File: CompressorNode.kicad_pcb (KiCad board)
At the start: 2 copper layers, 129.5 x 85.1 mm, 33 parts, among them J1 EXT1, J10 Screw_Terminal_01x03, J11 Screw_Terminal_01x02, J12 Screw_Terminal_01x03, J13 Screw_Terminal_01x04, J2 Screw_Terminal_01x04, J3 Screw_Terminal_01x03, J4 EXT2, J5 Screw_Terminal_01x02, J6 Screw_Terminal_01x02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

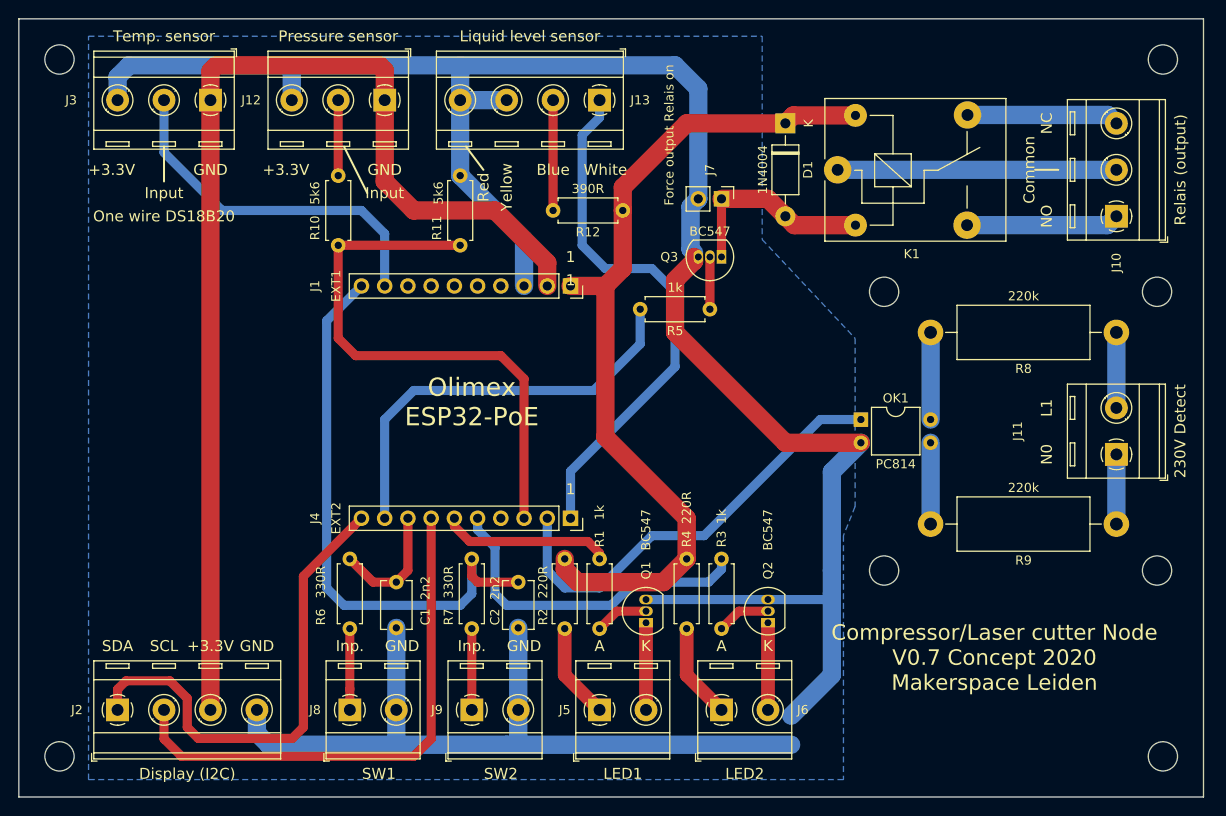
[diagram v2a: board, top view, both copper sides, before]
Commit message: LED Resistnow 47R to increase current for high power LEDs
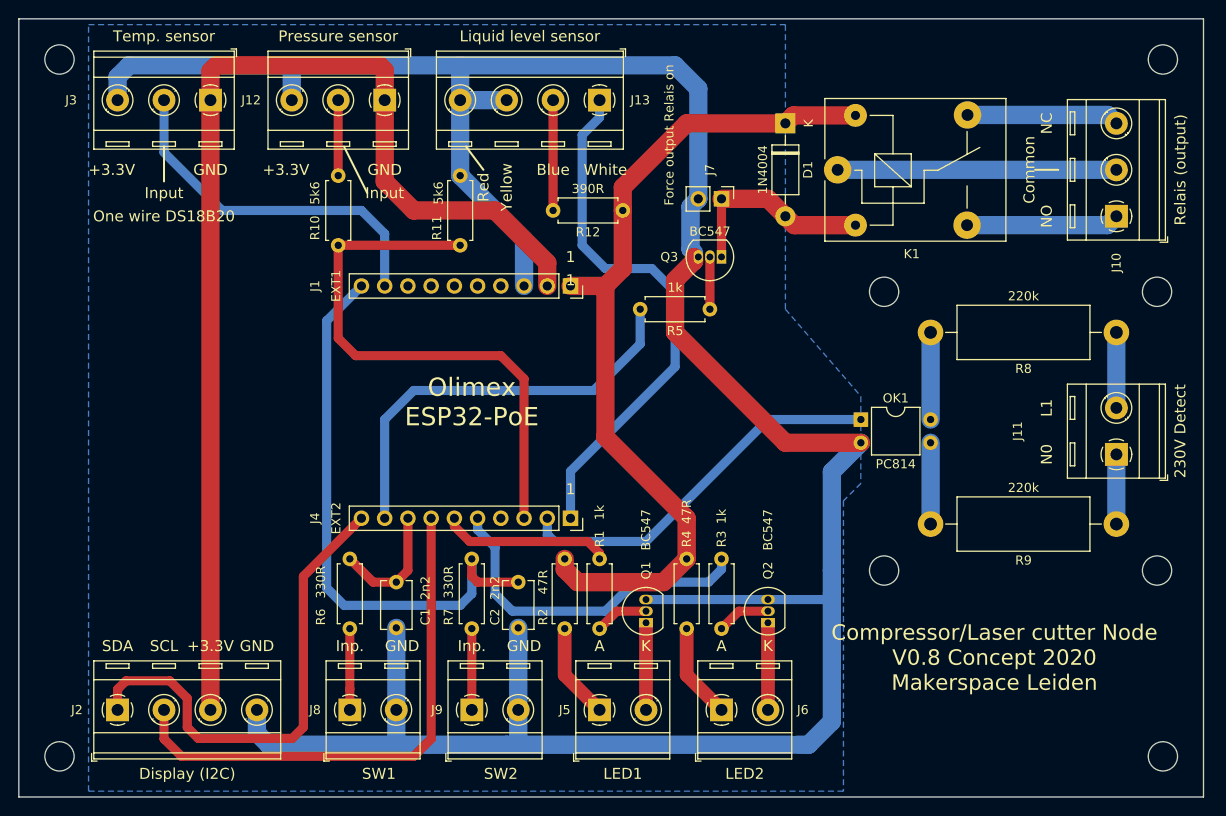
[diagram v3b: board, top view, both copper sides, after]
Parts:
- R2, R4: value 220R -> 47R
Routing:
- net GPI36_U1RXD: track 48.4 -> 42.0 mm
- net GND: track 297.1 -> 300.7 mm
- net GPIO33: track 37.1 -> 37.6 mm
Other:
- board text added: "Compressor/Laser cutter Node V0.8 Concept 2020 Makerspace Leiden"
- board text removed: "Compressor/Laser cutter Node V0.7 Concept 2020 Makerspace Leiden"
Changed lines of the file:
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@@
   (title_block
     (title CompressorNode)
-    (date 2020-03-29)
-    (rev "V0.7 Concept")
+    (date 2020-03-30)
+    (rev "V0.8 Concept")
     (company "MakerSpace Leiden")
     (comment 1 "Getekend door Hans Beerman")
@@
   )
   (setup
-    (last_trace_width 2)
+    (last_trace_width 0.25)
     (user_trace_width 0.5)
     (user_trace_width 0.75)
@@
     (add_net +3V3)
     (add_net +5V)
+    (add_net ESP_EN)
     (add_net GND)
+    (add_net GPI34_BUT1)
     (add_net GPI35)
     (add_net GPI36_U1RXD)
     (add_net GPI39)
+    (add_net GPIO0)
     (add_net GPIO13_I2C-SDA)
     (add_net GPIO14_HS2_CLK)
     (add_net GPIO15_HS2_CMD)
     (add_net GPIO16_I2C-SCL)
+    (add_net GPIO1_U0TXD)
+    (add_net GPIO2_HS2_DATA0)
     (add_net GPIO32)
     (add_net GPIO33)
+    (add_net GPIO3_U0RXD)
     (add_net GPIO4_U1TXD)
     (add_net GPIO5_SPI_C5)
@@
       (effects (font (size 1 1) (thickness 0.15)) (justify left))
     )
-    (fp_text value 220R (at -3.81 0 90) (layer F.SilkS)
+    (fp_text value 47R (at -3.81 0 90) (layer F.SilkS)
       (effects (font (size 1 1) (thickness 0.15)) (justify left))
     )
@@
       (effects (font (size 1 1) (thickness 0.15)))
     )
-    (fp_text value 220R (at 2.54 2.37 90) (layer F.SilkS)
+    (fp_text value 47R (at 2.54 2.37 90) (layer F.SilkS)
       (effects (font (size 1 1) (thickness 0.15)))
     )
@@
     (effects (font (size 1.2 1.2) (thickness 0.3)))
   )
-  (gr_text "Compressor/Laser cutter Node\nV0.7 Concept 2020\nMakerspace Leiden" (at 190.5 124.46) (layer F.SilkS)
+  (gr_text "Compressor/Laser cutter Node\nV0.8 Concept 2020\nMakerspace Leiden" (at 190.5 124.46) (layer F.SilkS)
     (effects (font (size 1.7 1.7) (thickness 0.4)))
   )
@@
   (segment (start 167.64 100.965) (end 155.575 88.9) (width 2) (layer F.Cu) (net 1))
   (segment (start 138.43 130.175) (end 138.43 121.205) (width 2) (layer B.Cu) (net 1))
-  (segment (start 168.275 130.81) (end 172.72 126.365) (width 2) (layer B.Cu) (net 1))
   (segment (start 172.72 104.14) (end 175.895 100.965) (width 2) (layer B.Cu) (net 1))
   (segment (start 138.43 130.175) (end 138.43 133.985) (width 2) (layer B.Cu) (net 1))
@@
   (segment (start 172.085 118.11) (end 172.72 117.475) (width 1) (layer B.Cu) (net 1))
   (segment (start 152.4 118.11) (end 172.085 118.11) (width 1) (layer B.Cu) (net 1))
-  (segment (start 172.72 126.365) (end 172.72 117.475) (width 2) (layer B.Cu) (net 1))
   (segment (start 172.72 117.475) (end 172.72 114.935) (width 2) (layer B.Cu) (net 1))
+  (segment (start 172.72 131.445) (end 172.72 117.475) (width 2) (layer B.Cu) (net 1))
+  (segment (start 168.91 133.985) (end 170.18 133.985) (width 2) (layer B.Cu) (net 1))
+  (segment (start 170.18 133.985) (end 172.72 131.445) (width 2) (layer B.Cu) (net 1))
   (segment (start 126.365 114.935) (end 125.095 116.205) (width 1) (layer F.Cu) (net 2))
   (segment (start 122.555 116.205) (end 120.015 113.665) (width 1) (layer F.Cu) (net 2))
@@
   (segment (start 147.32 113.03) (end 146.05 111.76) (width 1) (layer F.Cu) (net 11))
   (segment (start 133.985 110.49) (end 133.985 109.22) (width 1) (layer B.Cu) (net 12))
+  (segment (start 135.89 112.395) (end 133.985 110.49) (width 1) (layer B.Cu) (net 12))
   (segment (start 135.89 117.475) (end 135.89 112.395) (width 1) (layer B.Cu) (net 12))
   (segment (start 160.655 114.79637) (end 159.24637 116.205) (width 1) (layer B.Cu) (net 12))
+  (segment (start 147.955 119.38) (end 137.795 119.38) (width 1) (layer B.Cu) (net 12))
+  (segment (start 137.795 119.38) (end 135.89 117.475) (width 1) (layer B.Cu) (net 12))
+  (segment (start 159.24637 116.205) (end 151.13 116.205) (width 1) (layer B.Cu) (net 12))
   (segment (start 160.655 113.665) (end 160.655 114.79637) (width 1) (layer B.Cu) (net 12))
-  (segment (start 135.89 112.395) (end 133.985 110.49) (width 1) (layer B.Cu) (net 12))
-  (segment (start 159.24637 116.205) (end 151.13 116.205) (width 1) (layer B.Cu) (net 12))
-  (segment (start 151.13 116.205) (end 148.59 118.745) (width 1) (layer B.Cu) (net 12))
-  (segment (start 148.59 118.745) (end 137.16 118.745) (width 1) (layer B.Cu) (net 12))
-  (segment (start 137.16 118.745) (end 135.89 117.475) (width 1) (layer B.Cu) (net 12))
+  (segment (start 151.13 116.205) (end 147.955 119.38) (width 1) (layer B.Cu) (net 12))
   (segment (start 118.745 79.375) (end 132.08 79.375) (width 1) (layer F.Cu) (net 13))
   (segment (start 136.525 91.44) (end 139.065 93.98) (width 1) (layer F.Cu) (net 13))
@@
   (segment (start 118.745 89.535) (end 120.65 91.44) (width 1) (layer F.Cu) (net 13))
   (segment (start 141.605 110.422081) (end 141.605 109.22) (width 1) (layer B.Cu) (net 14))
-  (segment (start 141.605 114.935) (end 141.605 110.422081) (width 1) (layer B.Cu) (net 14))
-  (segment (start 171.45 98.425) (end 158.75 111.125) (width 1) (layer B.Cu) (net 14))
-  (segment (start 175.895 98.425) (end 171.45 98.425) (width 1) (layer B.Cu) (net 14))
-  (segment (start 158.75 111.125) (end 153.035 111.125) (width 1) (layer B.Cu) (net 14))
-  (segment (start 153.035 111.125) (end 147.32 116.84) (width 1) (layer B.Cu) (net 14))
-  (segment (start 143.51 116.84) (end 141.605 114.935) (width 1) (layer B.Cu) (net 14))
-  (segment (start 147.32 116.84) (end 143.51 116.84) (width 1) (layer B.Cu) (net 14))
+  (segment (start 175.895 98.425) (end 165.735 98.425) (width 1) (layer B.Cu) (net 14))
+  (segment (start 152.4 111.76) (end 142.385 111.76) (width 1) (layer B.Cu) (net 14))
+  (segment (start 142.385 111.76) (end 141.75 111.125) (width 1) (layer B.Cu) (net 14))
+  (segment (start 141.605 111.125) (end 141.605 110.422081) (width 1) (layer B.Cu) (net 14))
+  (segment (start 165.735 98.425) (end 152.4 111.76) (width 1) (layer B.Cu) (net 14))
+  (segment (start 141.75 111.125) (end 141.605 111.125) (width 1) (layer B.Cu) (net 14))
   (segment (start 147.32 65.405) (end 145.415 67.31) (width 1) (layer B.Cu) (net 15))
   (segment (start 145.415 79.375) (end 147.955 81.915) (width 1) (layer B.Cu) (net 15))
@@
     (polygon
       (pts
-        (xy 165.1 78.74) (xy 175.26 89.535) (xy 175.26 107.95) (xy 173.99 111.125) (xy 173.99 137.795)
-        (xy 91.44 137.795) (xy 91.44 56.515) (xy 165.1 56.515)
+        (xy 167.64 86.36) (xy 175.895 95.885) (xy 175.895 105.41) (xy 173.99 107.315) (xy 173.99 139.065)
+        (xy 91.44 139.065) (xy 91.44 55.245) (xy 167.64 55.245)
       )
     )

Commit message: Optocoupler was connected wrong
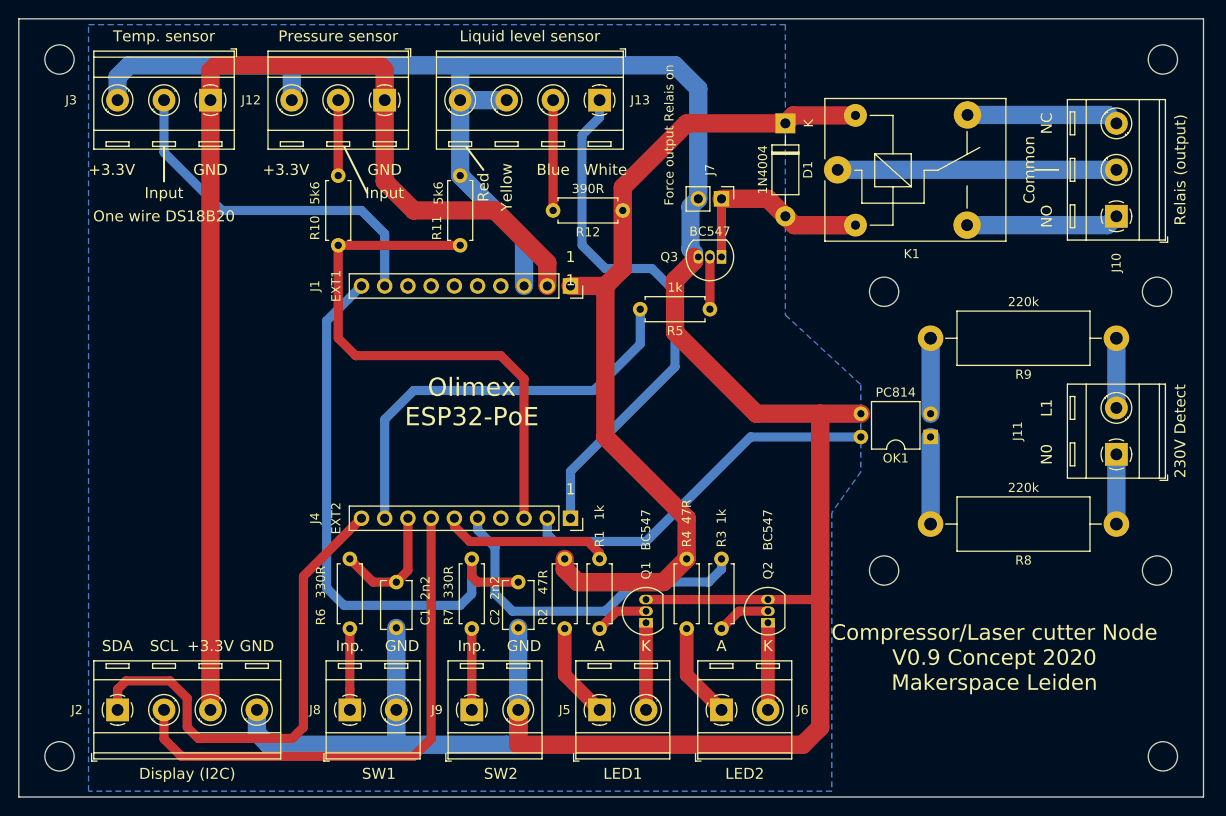
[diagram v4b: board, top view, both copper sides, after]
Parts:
- moved R8 21.0 mm to (203.8, 109.9)
- moved R9 20.3 mm to (203.8, 89.5)
- moved OK1 7.85 mm to (183.5, 100.3), turned to 180 degrees
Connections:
- OK1 pad 1: GPI36_U1RXD -> Net-(OK1-Pad1)
- OK1 pad 2: GND -> Net-(OK1-Pad2)
- OK1 pad 3: Net-(OK1-Pad3) -> GND
- OK1 pad 4: Net-(OK1-Pad4) -> GPI36_U1RXD
- R8 pad 1: Net-(J11-Pad2) -> Net-(J11-Pad1)
- R8 pad 2: Net-(OK1-Pad4) -> Net-(OK1-Pad1)
- R9 pad 1: Net-(J11-Pad1) -> Net-(J11-Pad2)
- R9 pad 2: Net-(OK1-Pad3) -> Net-(OK1-Pad2)
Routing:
- net Net-(OK1-Pad1): track 0.00 -> 9.53 mm
- net Net-(OK1-Pad4): track 9.52 -> 0.00 mm
- net Net-(OK1-Pad3): track 8.89 -> 0.00 mm
- net Net-(OK1-Pad2): track 0.00 -> 8.26 mm
- net GND: track 300.7 -> 303.3 mm
- net GPI36_U1RXD: track 42.0 -> 41.2 mm
- net Net-(J11-Pad2): track 8.25 -> 7.62 mm
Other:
- board text added: "Compressor/Laser cutter Node V0.9 Concept 2020 Makerspace Leiden"
- board text removed: "Compressor/Laser cutter Node V0.8 Concept 2020 Makerspace Leiden"

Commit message: R5 is now 150R because relais uses more current than expected
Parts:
- R5: value 1k -> 150R
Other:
- board text added: "Compressor/Laser cutter Node V0.10 Concept 2020 Makerspace Leiden"
- board text removed: "Compressor/Laser cutter Node V0.9 Concept 2020 Makerspace Leiden"
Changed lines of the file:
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@@
     (title CompressorNode)
     (date 2020-04-01)
-    (rev "V0.9 Concept")
+    (rev "V0.10 Concept")
     (company "MakerSpace Leiden")
     (comment 1 "Getekend door Hans Beerman")
@@
   )
   (setup
-    (last_trace_width 1)
+    (last_trace_width 0.25)
     (user_trace_width 0.5)
     (user_trace_width 0.75)
@@
       (effects (font (size 1 1) (thickness 0.15)))
     )
-    (fp_text value 1k (at 3.81 2.37) (layer F.SilkS)
+    (fp_text value 150R (at 3.81 2.37) (layer F.SilkS)
       (effects (font (size 1 1) (thickness 0.15)))
     )
@@
     (effects (font (size 1.2 1.2) (thickness 0.3)))
   )
-  (gr_text "Compressor/Laser cutter Node\nV0.9 Concept 2020\nMakerspace Leiden" (at 190.5 124.46) (layer F.SilkS)
+  (gr_text "Compressor/Laser cutter Node\nV0.10 Concept 2020\nMakerspace Leiden" (at 190.5 124.46) (layer F.SilkS)
     (effects (font (size 1.7 1.7) (thickness 0.4)))
   )

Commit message: resistor 4k7 added for DS18B20 temperature sensor
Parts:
- added R13: 4k7, Resistor_THT:R_Axial_DIN0207_L6.3mm_D2.5mm_P7.62mm_Horizontal, F.Cu at (128.3, 88.9)
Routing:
- net +3V3: track 125.5 -> 135.2 mm
- net GPIO4_U1TXD: track 39.2 -> 47.7 mm
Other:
- board text added: "Compressor/Laser cutter Node V0.11 Concept 2020 Makerspace Leiden"
- board text removed: "Compressor/Laser cutter Node V0.10 Concept 2020 Makerspace Leiden"
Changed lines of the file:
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@@
     (thickness 1.6)
     (drawings 59)
-    (tracks 170)
+    (tracks 176)
     (zones 0)
-    (modules 33)
+    (modules 34)
     (nets 34)
   )
@@
   (title_block
     (title CompressorNode)
-    (date 2020-04-01)
-    (rev "V0.10 Concept")
+    (date 2020-04-02)
+    (rev "V0.11 Concept")
     (company "MakerSpace Leiden")
     (comment 1 "Getekend door Hans Beerman")
@@
   )
   (setup
-    (last_trace_width 0.25)
+    (last_trace_width 1)
     (user_trace_width 0.5)
     (user_trace_width 0.75)
@@
     (add_net "Net-(Q2-Pad2)")
     (add_net "Net-(Q3-Pad2)")
+  )
+  (module Resistor_THT:R_Axial_DIN0207_L6.3mm_D2.5mm_P7.62mm_Horizontal (layer F.Cu)
+    (at 128.27 88.9)
+    (descr "Resistor, Axial_DIN0207 series, Axial, Horizontal, pin pitch=7.62mm, 0.25W = 1/4W, length*diameter=6.3*2.5mm^2, http://cdn-reichelt.de/documents/datenblatt/B400/1_4W%23YAG.pdf")
+    (tags "Resistor Axial_DIN0207 series Axial Horizontal pin pitch 7.62mm 0.25W = 1/4W length 6.3mm diameter 2.5mm")
+    (fp_text reference R13 (at 3.81 -2.37) (layer F.SilkS)
+      (effects (font (size 1 1) (thickness 0.15)))
+    )
+    (fp_text value 4k7 (at 3.81 2.37) (layer F.SilkS)
+      (effects (font (size 1 1) (thickness 0.15)))
+    )
+    (fp_text user %R (at 3.81 0) (layer F.Fab)
+      (effects (font (size 1 1) (thickness 0.15)))
+    )
+    (fp_line (start 8.67 -1.5) (end -1.05 -1.5) (layer F.CrtYd) (width 0.05))
+    (fp_line (start 8.67 1.5) (end 8.67 -1.5) (layer F.CrtYd) (width 0.05))
+    (fp_line (start -1.05 1.5) (end 8.67 1.5) (layer F.CrtYd) (width 0.05))
+    (fp_line (start -1.05 -1.5) (end -1.05 1.5) (layer F.CrtYd) (width 0.05))
+    (fp_line (start 7.08 1.37) (end 7.08 1.04) (layer F.SilkS) (width 0.12))
+    (fp_line (start 0.54 1.37) (end 7.08 1.37) (layer F.SilkS) (width 0.12))
+    (fp_line (start 0.54 1.04) (end 0.54 1.37) (layer F.SilkS) (width 0.12))
+    (fp_line (start 7.08 -1.37) (end 7.08 -1.04) (layer F.SilkS) (width 0.12))
+    (fp_line (start 0.54 -1.37) (end 7.08 -1.37) (layer F.SilkS) (width 0.12))
+    (fp_line (start 0.54 -1.04) (end 0.54 -1.37) (layer F.SilkS) (width 0.12))
+    (fp_line (start 7.62 0) (end 6.96 0) (layer F.Fab) (width 0.1))
+    (fp_line (start 0 0) (end 0.66 0) (layer F.Fab) (width 0.1))
+    (fp_line (start 6.96 -1.25) (end 0.66 -1.25) (layer F.Fab) (width 0.1))
+    (fp_line (start 6.96 1.25) (end 6.96 -1.25) (layer F.Fab) (width 0.1))
+    (fp_line (start 0.66 1.25) (end 6.96 1.25) (layer F.Fab) (width 0.1))
+    (fp_line (start 0.66 -1.25) (end 0.66 1.25) (layer F.Fab) (width 0.1))
+    (pad 2 thru_hole oval (at 7.62 0) (size 1.6 1.6) (drill 0.8) (layers *.Cu *.Mask)
+      (net 7 +3V3))
+    (pad 1 thru_hole circle (at 0 0) (size 1.6 1.6) (drill 0.8) (layers *.Cu *.Mask)
+      (net 6 GPIO4_U1TXD))
+    (model ${KISYS3DMOD}/Resistor_THT.3dshapes/R_Axial_DIN0207_L6.3mm_D2.5mm_P7.62mm_Horizontal.wrl
+      (at (xyz 0 0 0))
+      (scale (xyz 1 1 1))
+      (rotate (xyz 0 0 0))
+    )
   )
   (module Resistor_THT:R_Axial_DIN0207_L6.3mm_D2.5mm_P7.62mm_Horizontal (layer F.Cu)
@@
     (effects (font (size 1.2 1.2) (thickness 0.3)))
   )
-  (gr_text "Compressor/Laser cutter Node\nV0.10 Concept 2020\nMakerspace Leiden" (at 190.5 124.46) (layer F.SilkS)
+  (gr_text "Compressor/Laser cutter Node\nV0.11 Concept 2020\nMakerspace Leiden" (at 190.5 124.46) (layer F.SilkS)
     (effects (font (size 1.7 1.7) (thickness 0.4)))
   )
@@
   (segment (start 123.825 83.82) (end 123.825 78.105) (width 1) (layer B.Cu) (net 6))
   (segment (start 123.825 78.105) (end 121.285 75.565) (width 1) (layer B.Cu) (net 6))
+  (segment (start 125.73 88.9) (end 128.27 88.9) (width 1) (layer F.Cu) (net 6))
+  (segment (start 123.825 83.82) (end 123.825 86.995) (width 1) (layer F.Cu) (net 6))
+  (segment (start 123.825 86.995) (end 125.73 88.9) (width 1) (layer F.Cu) (net 6))
   (segment (start 123.825 60.25) (end 123.825 63.5) (width 2) (layer F.Cu) (net 7))
   (segment (start 123.265 59.69) (end 123.825 60.25) (width 2) (layer F.Cu) (net 7))
@@
   (segment (start 123.825 72.39) (end 127 75.565) (width 2) (layer F.Cu) (net 7))
   (segment (start 104.775 63.5) (end 104.775 130.175) (width 2) (layer F.Cu) (net 7))
+  (segment (start 141.605 86.995) (end 141.605 83.82) (width 1) (layer F.Cu) (net 7))
+  (segment (start 135.89 88.9) (end 139.7 88.9) (width 1) (layer F.Cu) (net 7))
+  (segment (start 139.7 88.9) (end 141.605 86.995) (width 1) (layer F.Cu) (net 7))
   (segment (start 128.905 133.35) (end 128.905 109.22) (width 1) (layer F.Cu) (net 8))
   (segment (start 127 135.255) (end 128.905 133.35) (width 1) (layer F.Cu) (net 8))
@@
     (polygon
       (pts
-        (xy 167.64 86.995) (xy 175.895 94.615) (xy 175.895 104.14) (xy 172.72 108.585) (xy 172.72 139.065)
+        (xy 167.64 81.28) (xy 175.895 92.075) (xy 175.895 104.775) (xy 172.72 108.585) (xy 172.72 139.065)
         (xy 91.44 139.065) (xy 91.44 55.245) (xy 167.64 55.245)
       )
